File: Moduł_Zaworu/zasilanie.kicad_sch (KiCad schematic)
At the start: 18 parts, among them J1 Screw_Terminal_01x02, J4 Screw_Terminal_01x02, U10 LD1117S33TR_SOT223, U3 TLV172IDCK, U4 TL431D, U9 L7805

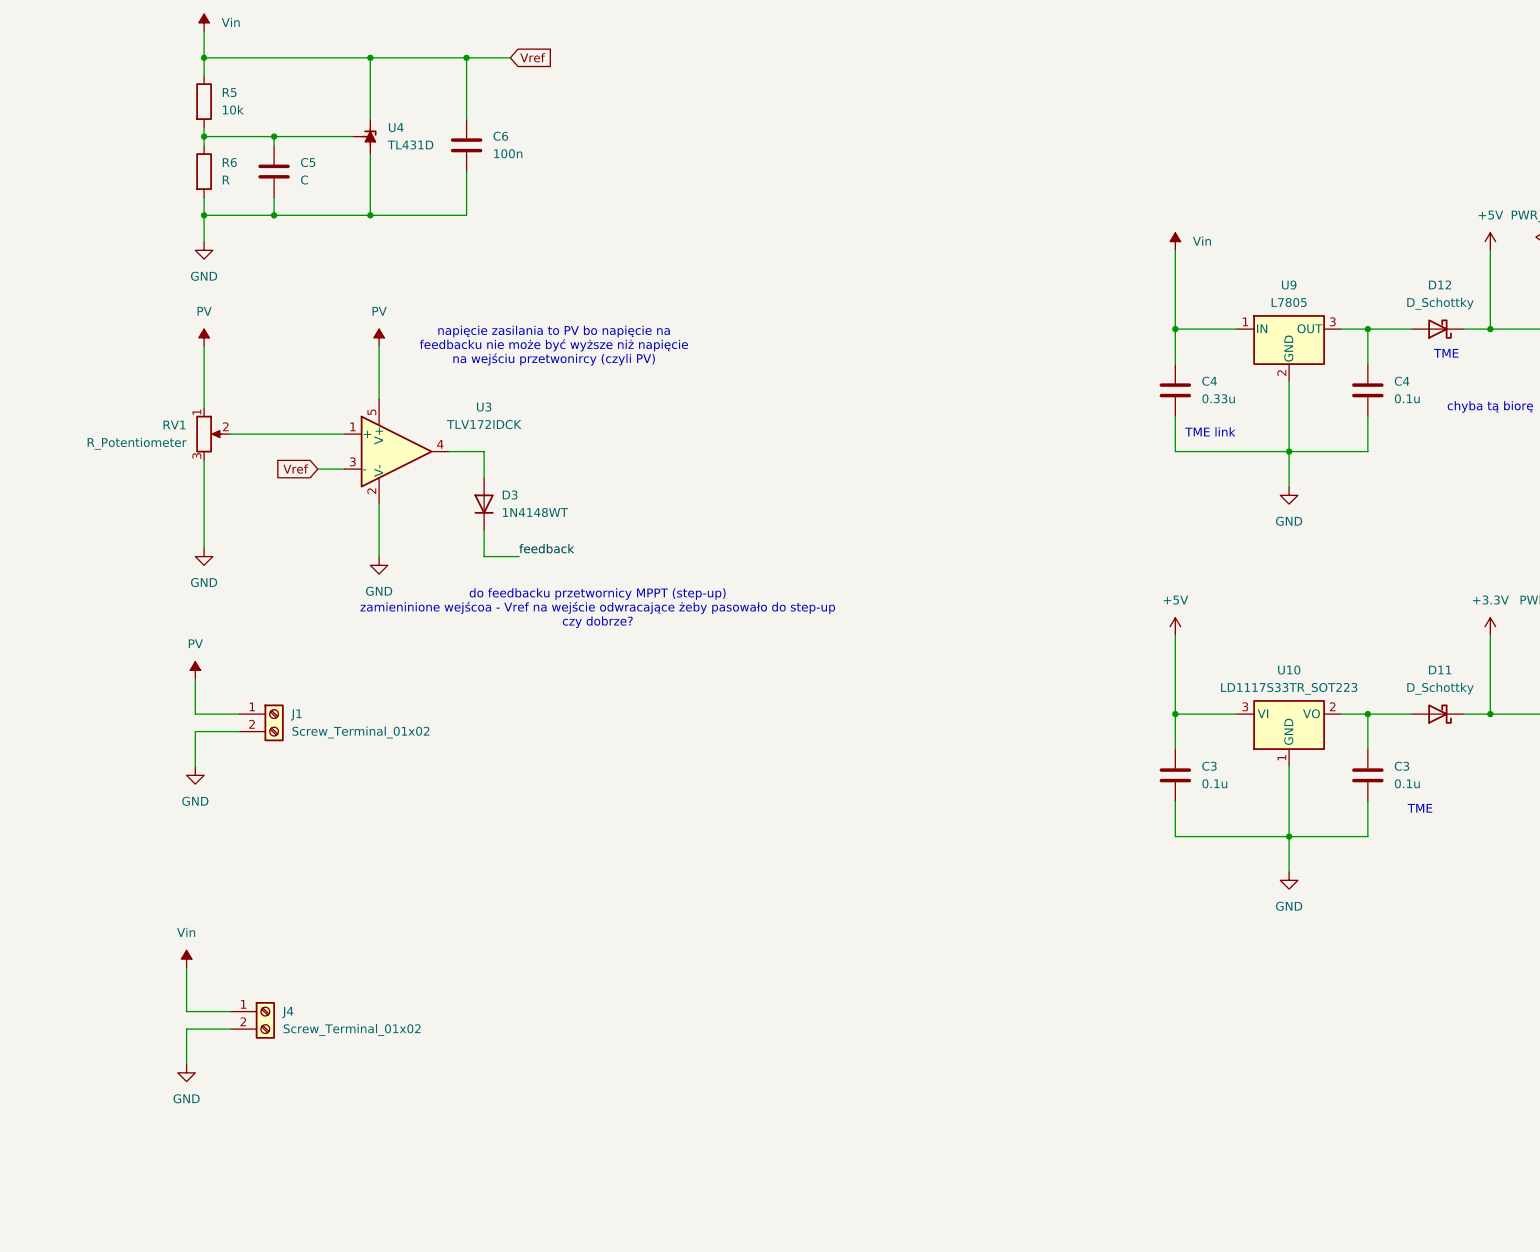
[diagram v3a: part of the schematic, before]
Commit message: Poprawki moduł zasilania, stowrzenie płytki, zostało trochę błędów, zapomniałem dać mouting holes
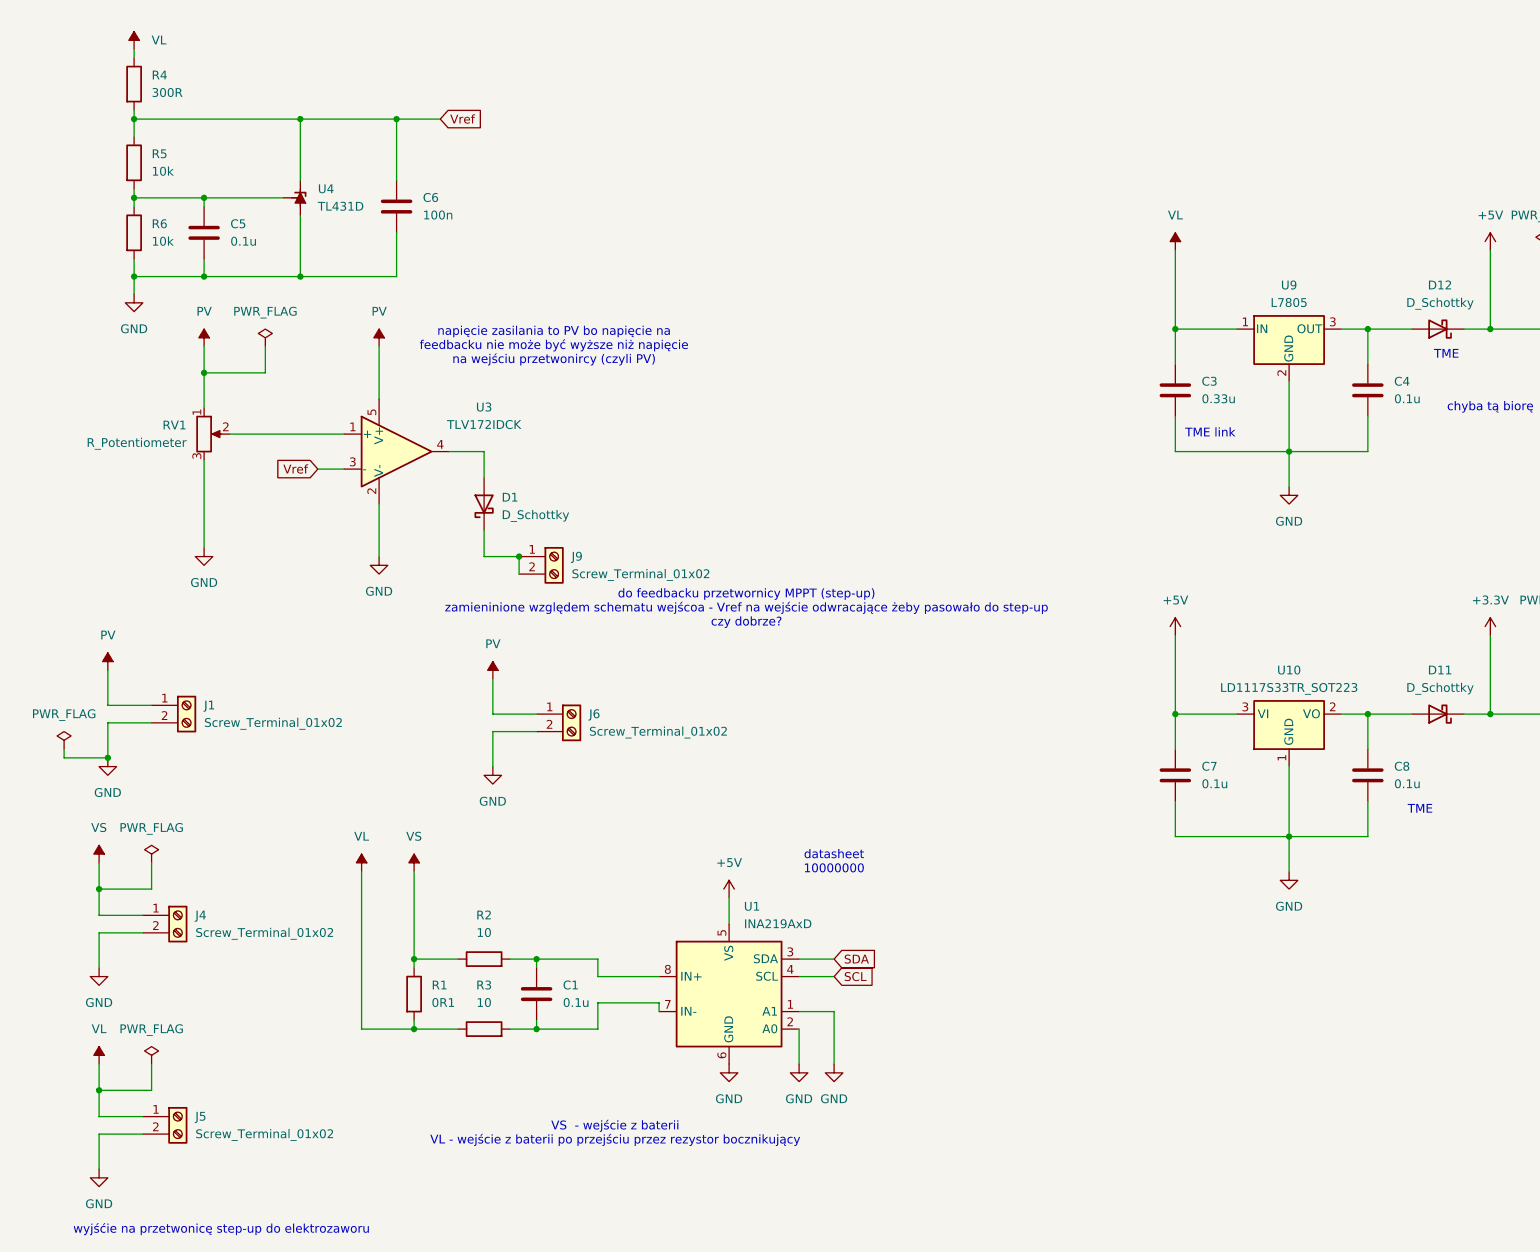
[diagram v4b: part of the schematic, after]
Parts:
- removed D3: 1N4148WT, Diode_SMD:D_SOD-523, symbol Diode:1N4148WT
- added C1: 0.1u, Capacitor_THT:C_Disc_D3.0mm_W1.6mm_P2.50mm, symbol Device:C
- added D1: D_Schottky, Diode_SMD:D_1206_3216Metric, symbol Device:D_Schottky
- added J5, J6: Screw_Terminal_01x02, TerminalBlock:TerminalBlock_MaiXu_MX126-5.0-02P_1x02_P5.00mm, symbol Connector:Screw_Terminal_01x02
- added J9: Screw_Terminal_01x02, TerminalBlock:TerminalBlock_Xinya_XY308-2.54-2P_1x02_P2.54mm_Horizontal, symbol Connector:Screw_Terminal_01x02
- added R1: 0R1, Resistor_SMD:R_1206_3216Metric, symbol Device:R
- added R2, R3: 10, Resistor_SMD:R_1206_3216Metric, symbol Device:R
- added R4: 300R, Resistor_SMD:R_1206_3216Metric, symbol Device:R
- added U1: INA219AxD, Package_SO:SOIC-8_3.9x4.9mm_P1.27mm, symbol Sensor_Energy:INA219AxD
- C5: value C -> 0.1u; footprint (none) -> Capacitor_THT:C_Disc_D3.0mm_W1.6mm_P2.50mm
- C6: footprint (none) -> Capacitor_THT:C_Disc_D3.0mm_W1.6mm_P2.50mm
- R5: footprint (none) -> Resistor_SMD:R_1206_3216Metric
- R6: value R -> 10k; footprint (none) -> Resistor_SMD:R_1206_3216Metric
- RV1: footprint (none) -> Potentiometer_THT:Potentiometer_Bourns_3386W_Horizontal
- U3: footprint Package_TO_SOT_SMD:SOT-353_SC-70-5 -> Package_SO:SOIC-8_5.3x5.3mm_P1.27mm
- renumbered C4 to C3, C3 to C7, C3 to C8
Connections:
- net +5V: now also U1.5 (VS)
- net GND: now also J5.2 (Pin_2), J6.2 (Pin_2), U1.1 (A1), U1.2 (A0), U1.6 (GND)
- net PV: now also J6.1 (Pin_1)
- net at U3.4: now also D1.2 (A)
- net Vin renamed Vref
- net Vref: now also R4.2; no longer C3.1, J4.1 (Pin_1), U9.1 (IN)
- new net: C1.1, R2.2, U1.8 (IN+)
- new net: D1.1 (K), J9.1 (Pin_1), J9.2 (Pin_2)
- new net: C1.2, R3.2, U1.7 (IN-)
- new net SCL: U1.4 (SCL)
- new net SDA: U1.3 (SDA)
- new net VL: C3.1, J5.1 (Pin_1), R1.2, R3.1, R4.1, U9.1 (IN)
- new net VS: J4.1 (Pin_1), R1.1, R2.1
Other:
- note added: "VS - wejście z baterii VL - wejście z baterii po przejściu przez rezystor bocznikujący"
- note added: "datasheet 10000000"
- note added: "do feedbacku przetwornicy MPPT (step-up) zamieninione względem schematu wejścoa - Vref na wejście odwracające żeby pasowało do step-up czy dobrze?"
- note added: "wyjśćie na przetwonicę step-up do elektrozaworu"
- note removed: "do feedbacku przetwornicy MPPT (step-up) zamieninione wejścoa - Vref na wejście odwracające żeby pasowało do step-up czy dobrze?"
- moved on the sheet: C5, C6, J1, J4, R5, R6, U4

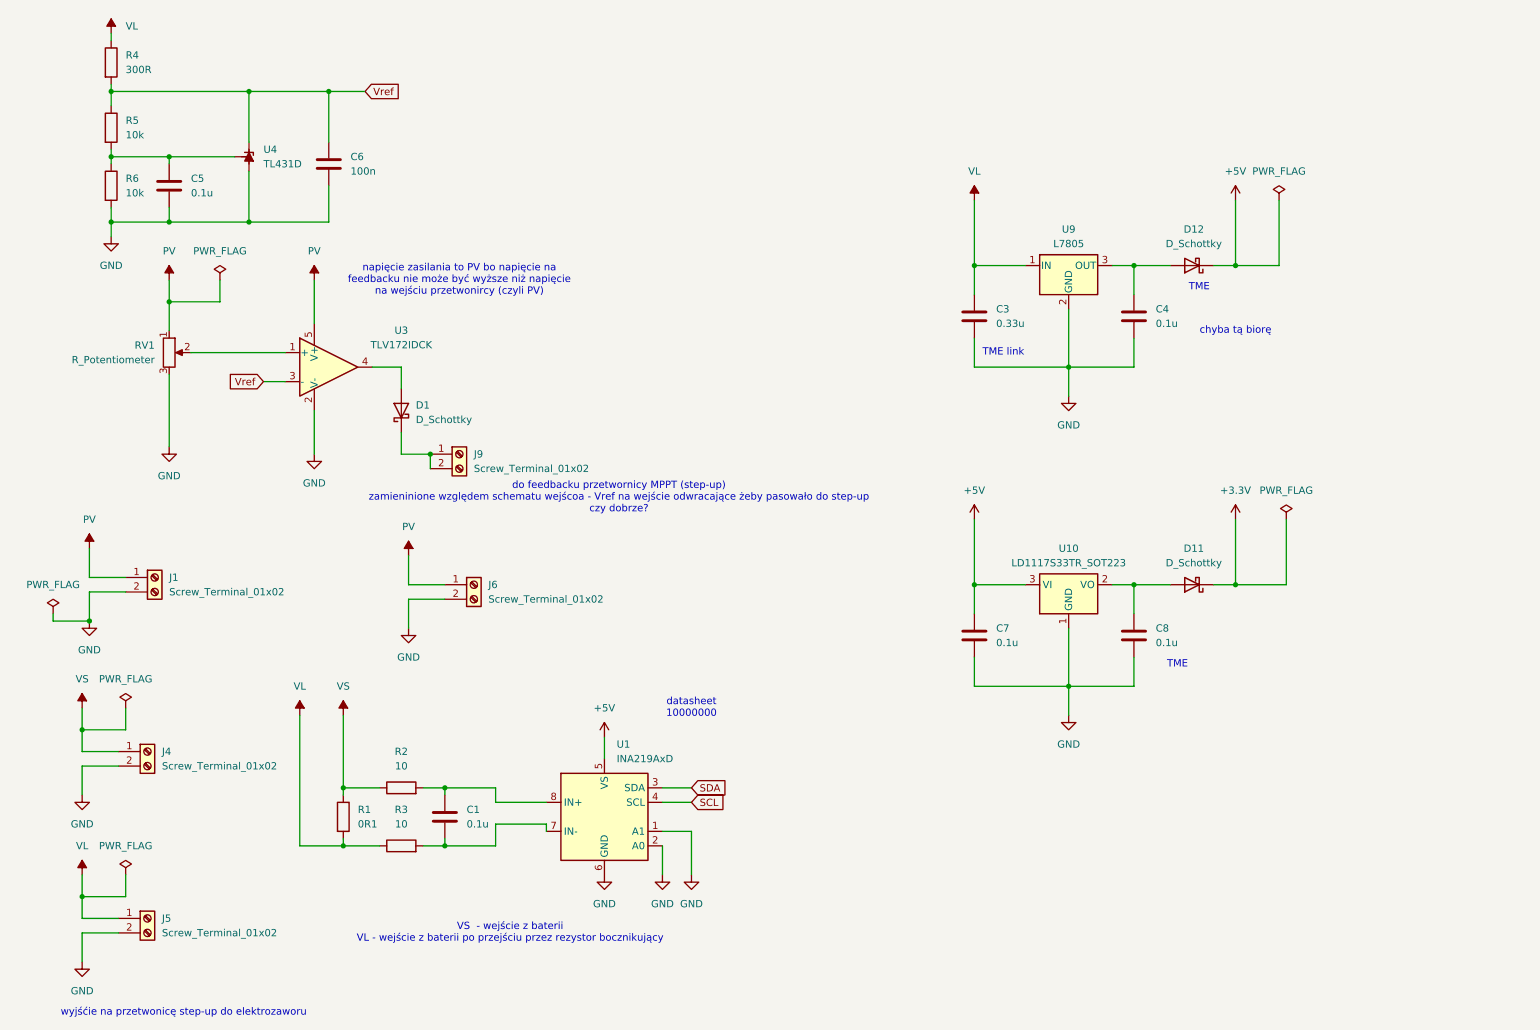
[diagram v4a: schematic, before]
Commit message: Gotowy do zatwierdzenia moduł zasilaina
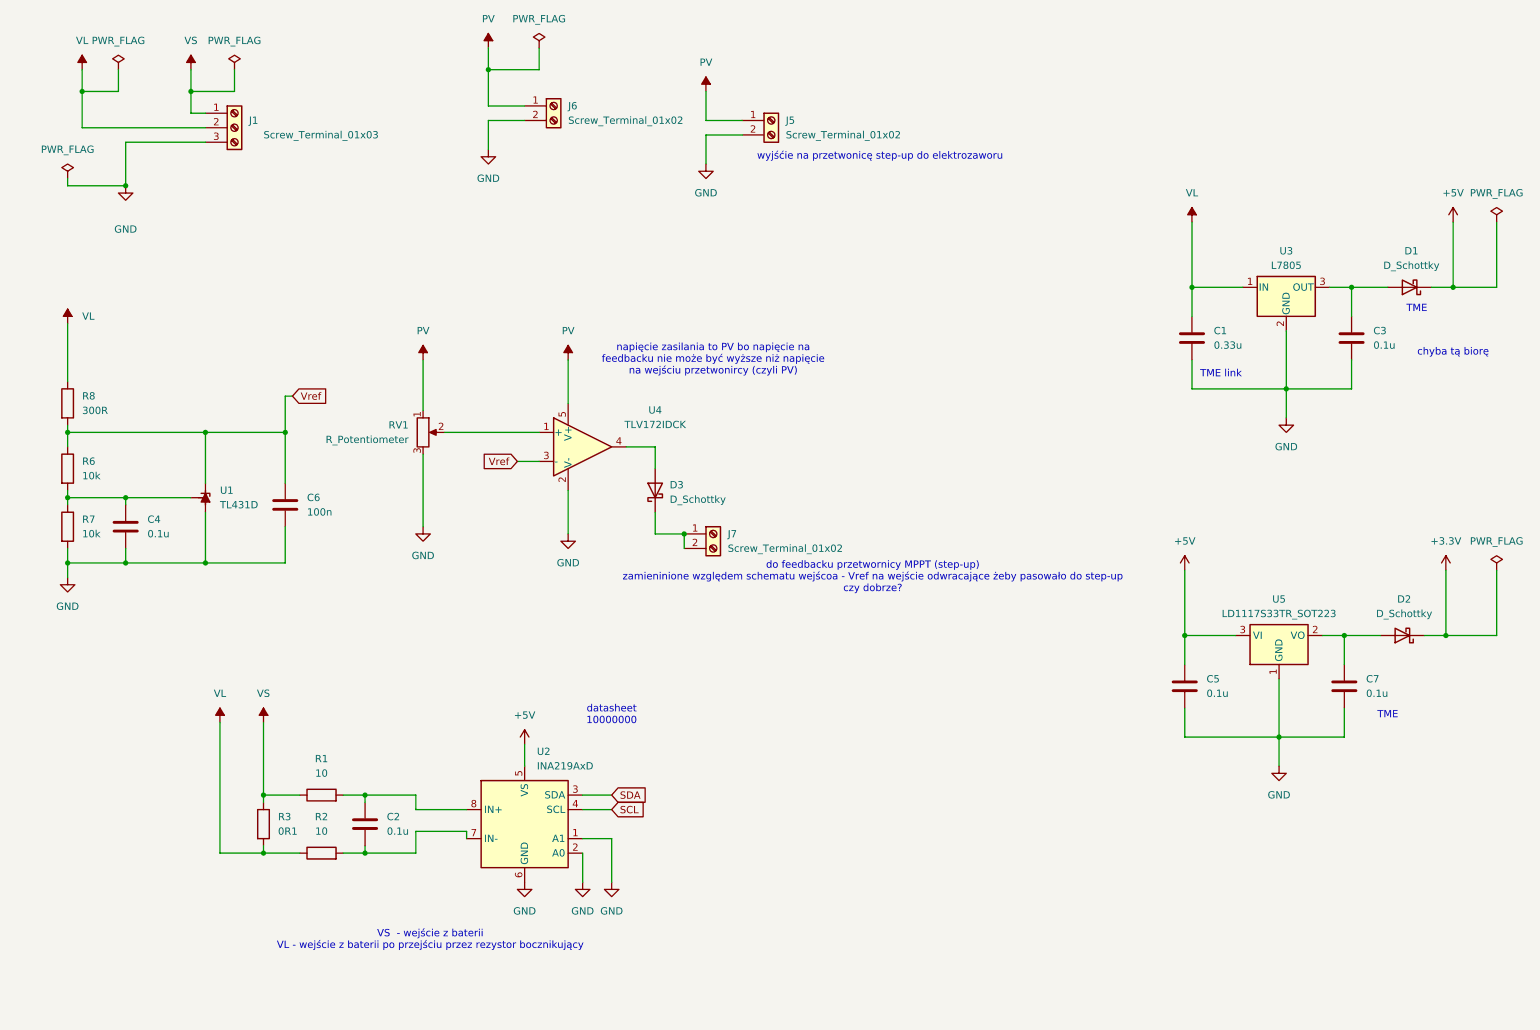
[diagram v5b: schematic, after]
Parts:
- removed J4, J5: Screw_Terminal_01x02, TerminalBlock:TerminalBlock_MaiXu_MX126-5.0-02P_1x02_P5.00mm, symbol Connector:Screw_Terminal_01x02
- added J1: Screw_Terminal_01x03, TerminalBlock:TerminalBlock_MaiXu_MX126-5.0-03P_1x03_P5.00mm, symbol Connector:Screw_Terminal_01x03
- renumbered C3 to C1, C1 to C2, C4 to C3, C5 to C4, C7 to C5, C8 to C7, D12 to D1, D11 to D2, D1 to D3, J6 to J5, J1 to J6, J9 to J7, R2 to R1, R3 to R2, R1 to R3, R5 to R6, R6 to R7, R4 to R8, U4 to U1, U1 to U2, U9 to U3, U3 to U4, U10 to U5
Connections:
- net GND: now also J1.3 (Pin_3)
- net VL: now also J1.2 (Pin_2)
- net VS: now also J1.1 (Pin_1)
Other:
- moved on the sheet: C1, C2, C3, C4, C5, C6, C7, D1, D2, D3, J5, J6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
